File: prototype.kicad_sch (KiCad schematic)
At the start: 20 parts, among them CON1 SNES-CONN, IC1 SN74LVC4245A, IC2 SN74LVC4245A, IC3 SN74LVC4245A, IC4 SN74LVC4245A, IC5 SN74LVC4245A, IC6 SN74LVC4245A, IC7 SN74LVC4245A, U1 AMS1117-3.3

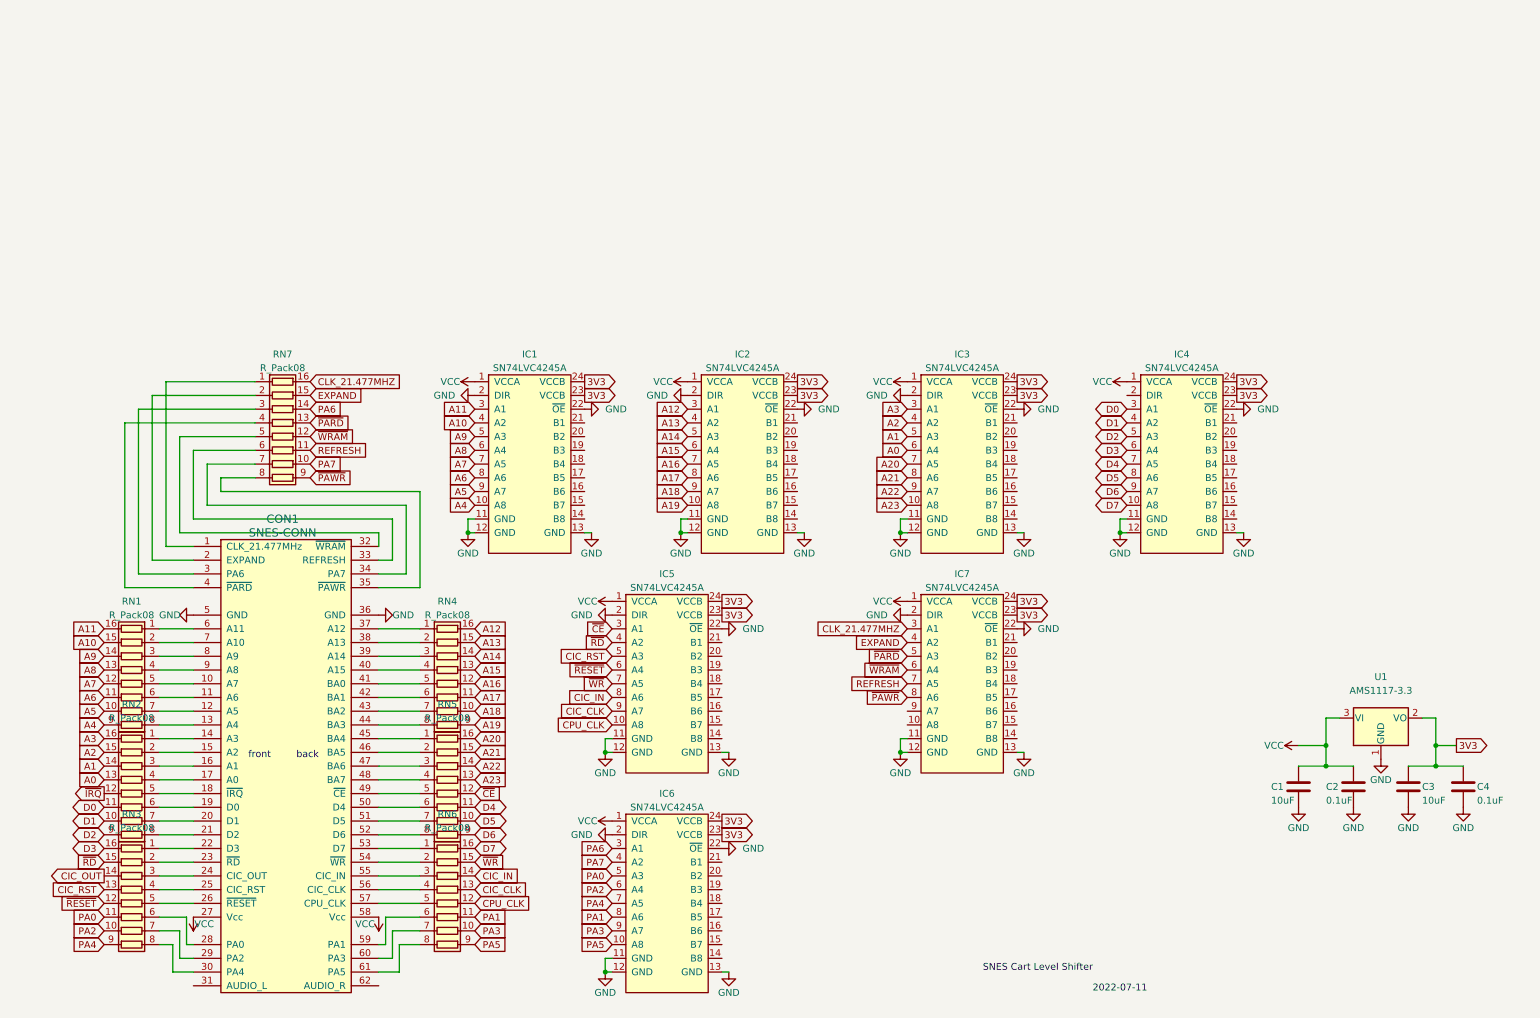
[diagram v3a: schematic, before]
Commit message: Redesign to reduce components, include PIC12 for CIC implementation
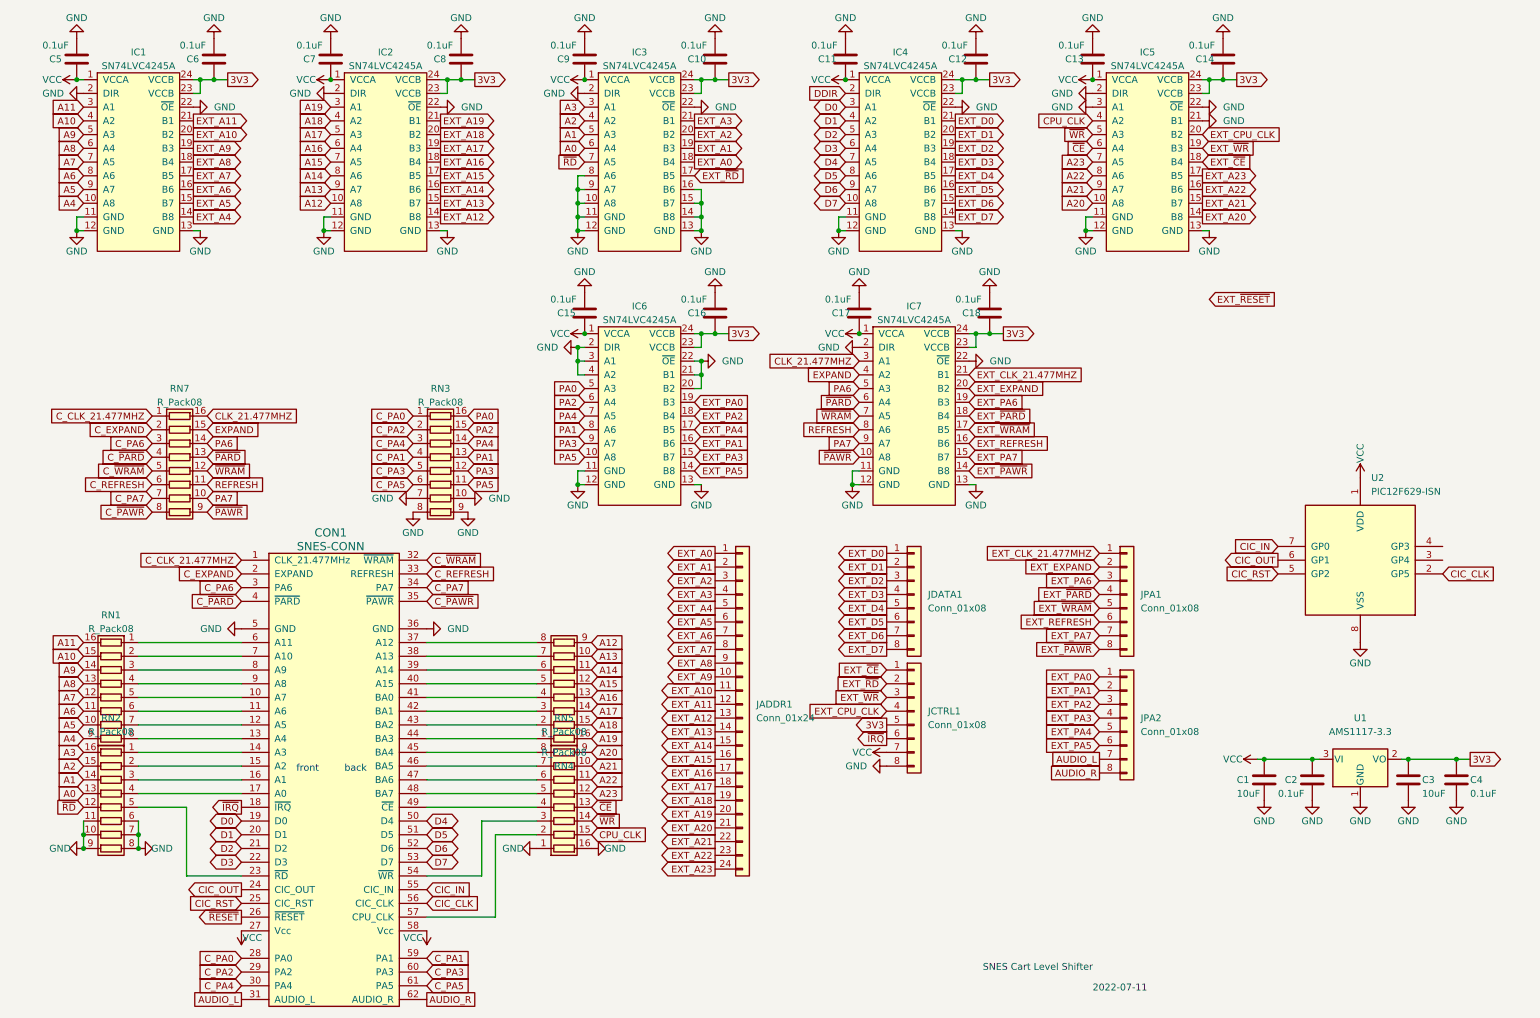
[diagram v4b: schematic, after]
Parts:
- removed RN6: R_Pack08, Package_SO:SOIC-16_3.9x9.9mm_P1.27mm, symbol Device:R_Pack08
- added C10, C11, C12, C13, C14, C15, C16, C17, C18, C5, C6, C7, C8, C9: 0.1uF, Capacitor_SMD:C_0805_2012Metric_Pad1.18x1.45mm_HandSolder, symbol Device:C
- added JADDR1: Conn_01x24, Connector_PinHeader_2.54mm:PinHeader_1x24_P2.54mm_Horizontal, symbol Connector_Generic:Conn_01x24
- added JCTRL1, JDATA1, JPA1, JPA2: Conn_01x08, Connector_PinHeader_2.54mm:PinHeader_1x08_P2.54mm_Horizontal, symbol Connector_Generic:Conn_01x08
- added U2: PIC12F629-ISN, Package_DIP:DIP-8_W7.62mm, symbol MCU_Microchip_PIC12:PIC12F629-ISN
- C1, C2, C3, C4: footprint Capacitor_SMD:C_1206_3216Metric -> Capacitor_SMD:C_0805_2012Metric_Pad1.18x1.45mm_HandSolder
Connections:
- net 3V3: now also C10.1, C12.1, C14.1, C16.1, C18.1, C6.1, C8.1, JCTRL1.5 (Pin_5)
- net A12: now also IC2.10 (A8), RN4.9 (R8.2); no longer IC2.3 (A1), RN4.16 (R1.2)
- net A13: now also IC2.9 (A7), RN4.10 (R7.2); no longer IC2.4 (A2), RN4.15 (R2.2)
- net A14: now also IC2.8 (A6), RN4.11 (R6.2); no longer IC2.5 (A3), RN4.14 (R3.2)
- net A15: now also IC2.7 (A5), RN4.12 (R5.2); no longer IC2.6 (A4), RN4.13 (R4.2)
- net A16: now also IC2.6 (A4), RN4.13 (R4.2); no longer IC2.7 (A5), RN4.12 (R5.2)
- net A17: now also IC2.5 (A3), RN4.14 (R3.2); no longer IC2.8 (A6), RN4.11 (R6.2)
- net A18: now also IC2.4 (A2), RN4.15 (R2.2); no longer IC2.9 (A7), RN4.10 (R7.2)
- net A19: now also IC2.3 (A1), RN4.16 (R1.2); no longer IC2.10 (A8), RN4.9 (R8.2)
- net A20: now also IC5.10 (A8), RN5.9 (R8.2); no longer IC3.7 (A5), RN5.16 (R1.2)
- net A21: now also IC5.9 (A7), RN5.10 (R7.2); no longer IC3.8 (A6), RN5.15 (R2.2)
- net A22: now also IC5.8 (A6), RN5.11 (R6.2); no longer IC3.9 (A7), RN5.14 (R3.2)
- net A23: now also IC5.7 (A5), RN5.12 (R5.2); no longer IC3.10 (A8), RN5.13 (R4.2)
- net CIC_CLK: now also CON1.56 (CIC_CLK), U2.2 (GP5); no longer IC5.9 (A7)
- net CIC_IN: now also CON1.55 (CIC_IN), U2.7 (GP0); no longer IC5.8 (A6)
- net CIC_OUT: now also CON1.24 (CIC_OUT), U2.6 (GP1); no longer RN3.14 (R3.2)
- net CIC_RST: now also CON1.25 (CIC_RST), U2.5 (GP2); no longer IC5.5 (A3), RN3.13 (R4.2)
- net CPU_CLK: now also IC5.4 (A2), RN5.15 (R2.2); no longer IC5.10 (A8)
- net D0: now also CON1.19 (D0); no longer RN2.11 (R6.2)
- net D1: now also CON1.20 (D1); no longer RN2.10 (R7.2)
- net D2: now also CON1.21 (D2); no longer RN2.9 (R8.2)
- net D3: now also CON1.22 (D3); no longer RN3.16 (R1.2)
- net D4: now also CON1.50 (D4); no longer RN5.11 (R6.2)
- net D5: now also CON1.51 (D5); no longer RN5.10 (R7.2)
- net D6: now also CON1.52 (D6); no longer RN5.9 (R8.2)
- net D7: now also CON1.53 (D7)
- net GND: now also IC3.10 (A8), IC3.14 (B8), IC3.15 (B7), IC3.16 (B6), IC3.8 (A6), IC3.9 (A7), IC5.21 (B1), IC5.3 (A1), IC6.20 (B2), IC6.21 (B1), IC6.3 (A1), IC6.4 (A2), RN2.10 (R7.2), RN2.11 (R6.2), RN2.6 (R6.1), RN2.7 (R7.1), RN2.8 (R8.1), RN2.9 (R8.2), RN3.10 (R7.2), RN3.7 (R7.1), RN3.8 (R8.1), RN3.9 (R8.2), RN5.1 (R1.1), RN5.16 (R1.2), C10.2, C11.2, C12.2, C13.2, C14.2, C15.2, C16.2, C17.2, C18.2, C5.2, C6.2, C7.2, C8.2, C9.2, JCTRL1.8 (Pin_8), U2.8 (VSS)
- net PA0: now also RN3.16 (R1.2); no longer RN3.11 (R6.2)
- net PA1: now also RN3.13 (R4.2)
- net PA2: now also RN3.15 (R2.2); no longer RN3.10 (R7.2)
- net PA3: now also RN3.12 (R5.2)
- net PA4: now also RN3.14 (R3.2); no longer RN3.9 (R8.2)
- net PA5: now also RN3.11 (R6.2)
- net PA6: now also IC7.5 (A3); no longer IC6.3 (A1)
- net PA7: now also IC7.9 (A7); no longer IC6.4 (A2)
- net REFRESH: now also IC7.8 (A6); no longer IC7.7 (A5)
- net VCC: now also C11.1, C13.1, C15.1, C17.1, C5.1, C7.1, C9.1, JCTRL1.7 (Pin_7), U2.1 (VDD)
- net ~{CE}: now also IC5.6 (A4), RN5.13 (R4.2); no longer IC5.3 (A1), RN5.12 (R5.2)
- net ~{IRQ}: now also CON1.18 (~{IRQ}), JCTRL1.6 (Pin_6); no longer RN2.12 (R5.2)
- net ~{PARD}: now also IC7.6 (A4); no longer IC7.5 (A3)
- net ~{PAWR}: now also IC7.10 (A8); no longer IC7.8 (A6)
- net ~{RD}: now also IC3.7 (A5), RN2.12 (R5.2); no longer IC5.4 (A2), RN3.15 (R2.2)
- net ~{RESET}: now also CON1.26 (~{RESET}); no longer IC5.6 (A4), RN3.12 (R5.2)
- net ~{WRAM}: now also IC7.7 (A5); no longer IC7.6 (A4)
- net ~{WR}: now also IC5.5 (A3), RN5.14 (R3.2); no longer IC5.7 (A5)
- net EXT_A20: now reaches IC5.14 (B8)
- net EXT_A20: now also JADDR1.21 (Pin_21)
- net EXT_A21: now reaches IC5.15 (B7)
- net EXT_A21: now also JADDR1.22 (Pin_22)
- net EXT_A22: now reaches IC5.16 (B6)
- net EXT_A22: now also JADDR1.23 (Pin_23)
- net EXT_A23: now reaches IC5.17 (B5)
- net EXT_A23: now also JADDR1.24 (Pin_24)
- net EXT_~{CE}: now reaches IC5.18 (B4)
- net EXT_~{CE}: now also JCTRL1.1 (Pin_1)
- net EXT_~{WR}: now reaches IC5.19 (B3)
- net EXT_~{WR}: now also JCTRL1.3 (Pin_3)
- net EXT_CPU_CLK: now reaches IC5.20 (B2)
- net EXT_CPU_CLK: now also JCTRL1.4 (Pin_4)
- net C_CLK_21.477MHZ: now reaches CON1.1 (CLK_21.477MHz), RN7.1 (R1.1)
- net at RN2.5 (R5.1): now also CON1.23 (~{RD}); no longer CON1.18 (~{IRQ})
- net C_EXPAND: now reaches CON1.2 (EXPAND), RN7.2 (R2.1)
- net C_PA0: now reaches RN3.1 (R1.1)
- net C_PA0: now also CON1.28 (PA0); no longer CON1.22 (D3)
- net C_PA2: now reaches RN3.2 (R2.1)
- net C_PA2: now also CON1.29 (PA2); no longer CON1.23 (~{RD})
- net C_PA4: now reaches RN3.3 (R3.1)
- net C_PA4: now also CON1.30 (PA4); no longer CON1.24 (CIC_OUT)
- net C_PA1: now reaches RN3.4 (R4.1)
- net C_PA1: now also CON1.59 (PA1); no longer CON1.25 (CIC_RST)
- net C_PA3: now reaches RN3.5 (R5.1)
- net C_PA3: now also CON1.60 (PA3); no longer CON1.26 (~{RESET})
- net C_PA5: now reaches RN3.6 (R6.1)
- net C_PA5: now also CON1.61 (PA5); no longer CON1.28 (PA0)
- net C_PA6: now reaches CON1.3 (PA6), RN7.3 (R3.1)
- net AUDIO_L: now reaches CON1.31 (AUDIO_L)
- net AUDIO_L: now also JPA2.7 (Pin_7)
- net C_~{WRAM}: now reaches CON1.32 (~{WRAM}), RN7.5 (R5.1)
- net C_REFRESH: now reaches CON1.33 (REFRESH), RN7.6 (R6.1)
- net C_PA7: now reaches CON1.34 (PA7), RN7.7 (R7.1)
- net C_~{PAWR}: now reaches CON1.35 (~{PAWR}), RN7.8 (R8.1)
- net at CON1.37 (A12): now also RN4.8 (R8.1); no longer RN4.1 (R1.1)
- net at CON1.38 (A13): now also RN4.7 (R7.1); no longer RN4.2 (R2.1)
- net at CON1.39 (A14): now also RN4.6 (R6.1); no longer RN4.3 (R3.1)
- net C_~{PARD}: now reaches CON1.4 (~{PARD}), RN7.4 (R4.1)
- net at CON1.40 (A15): now also RN4.5 (R5.1); no longer RN4.4 (R4.1)
- net at CON1.41 (BA0): now also RN4.4 (R4.1); no longer RN4.5 (R5.1)
- net at CON1.42 (BA1): now also RN4.3 (R3.1); no longer RN4.6 (R6.1)
- net at CON1.43 (BA2): now also RN4.2 (R2.1); no longer RN4.7 (R7.1)
- net at CON1.44 (BA3): now also RN4.1 (R1.1); no longer RN4.8 (R8.1)
- net at CON1.45 (BA4): now also RN5.8 (R8.1); no longer RN5.1 (R1.1)
- net at CON1.46 (BA5): now also RN5.7 (R7.1); no longer RN5.2 (R2.1)
- net at CON1.47 (BA6): now also RN5.6 (R6.1); no longer RN5.3 (R3.1)
- net at CON1.48 (BA7): now also RN5.5 (R5.1); no longer RN5.4 (R4.1)
- net at CON1.49 (~{CE}): now also RN5.4 (R4.1); no longer RN5.5 (R5.1)
- net at CON1.54 (~{WR}): now also RN5.3 (R3.1)
- net at CON1.57 (CPU_CLK): now also RN5.2 (R2.1)
- net AUDIO_R: now reaches CON1.62 (AUDIO_R)
- net AUDIO_R: now also JPA2.8 (Pin_8)
- net EXT_D7: now reaches IC4.14 (B8)
- net EXT_D7: now also JDATA1.8 (Pin_8)
- net EXT_D6: now reaches IC4.15 (B7)
- net EXT_D6: now also JDATA1.7 (Pin_7)
- net EXT_D5: now reaches IC4.16 (B6)
- net EXT_D5: now also JDATA1.6 (Pin_6)
- net EXT_D4: now reaches IC4.17 (B5)
- net EXT_D4: now also JDATA1.5 (Pin_5)
- net EXT_D3: now reaches IC4.18 (B4)
- net EXT_D3: now also JDATA1.4 (Pin_4)
- net EXT_D2: now reaches IC4.19 (B3)
- net EXT_D2: now also JDATA1.3 (Pin_3)
- net DDIR: now reaches IC4.2 (DIR)
- net EXT_D1: now reaches IC4.20 (B2)
- net EXT_D1: now also JDATA1.2 (Pin_2)
- net EXT_D0: now reaches IC4.21 (B1)
- net EXT_D0: now also JDATA1.1 (Pin_1)
- net EXT_A4: now reaches IC1.14 (B8)
- net EXT_A4: now also JADDR1.5 (Pin_5)
- net EXT_A5: now reaches IC1.15 (B7)
- net EXT_A5: now also JADDR1.6 (Pin_6)
- net EXT_A6: now reaches IC1.16 (B6)
- net EXT_A6: now also JADDR1.7 (Pin_7)
- net EXT_A7: now reaches IC1.17 (B5)
- net EXT_A7: now also JADDR1.8 (Pin_8)
- net EXT_A8: now reaches IC1.18 (B4)
- net EXT_A8: now also JADDR1.9 (Pin_9)
- net EXT_A9: now reaches IC1.19 (B3)
- net EXT_A9: now also JADDR1.10 (Pin_10)
- net EXT_A10: now reaches IC1.20 (B2)
- net EXT_A10: now also JADDR1.11 (Pin_11)
- net EXT_A11: now reaches IC1.21 (B1)
- net EXT_A11: now also JADDR1.12 (Pin_12)
- net EXT_A12: now reaches IC2.14 (B8)
- net EXT_A12: now also JADDR1.13 (Pin_13)
- net EXT_A13: now reaches IC2.15 (B7)
- net EXT_A13: now also JADDR1.14 (Pin_14)
- net EXT_A14: now reaches IC2.16 (B6)
- net EXT_A14: now also JADDR1.15 (Pin_15)
- net EXT_A15: now reaches IC2.17 (B5)
- net EXT_A15: now also JADDR1.16 (Pin_16)
- net EXT_A16: now reaches IC2.18 (B4)
- net EXT_A16: now also JADDR1.17 (Pin_17)
- net EXT_A17: now reaches IC2.19 (B3)
- net EXT_A17: now also JADDR1.18 (Pin_18)
- net EXT_A18: now reaches IC2.20 (B2)
- net EXT_A18: now also JADDR1.19 (Pin_19)
- net EXT_A19: now reaches IC2.21 (B1)
- net EXT_A19: now also JADDR1.20 (Pin_20)
- net EXT_~{PAWR}: now reaches IC7.14 (B8)
- net EXT_~{PAWR}: now also JPA1.8 (Pin_8)
- net EXT_PA7: now reaches IC7.15 (B7)
- net EXT_PA7: now also JPA1.7 (Pin_7)
- net EXT_REFRESH: now reaches IC7.16 (B6)
- net EXT_REFRESH: now also JPA1.6 (Pin_6)
- net EXT_~{WRAM}: now reaches IC7.17 (B5)
- net EXT_~{WRAM}: now also JPA1.5 (Pin_5)
- net EXT_~{PARD}: now reaches IC7.18 (B4)
- net EXT_~{PARD}: now also JPA1.4 (Pin_4)
- net EXT_PA6: now reaches IC7.19 (B3)
- net EXT_PA6: now also JPA1.3 (Pin_3)
- net EXT_EXPAND: now reaches IC7.20 (B2)
- net EXT_EXPAND: now also JPA1.2 (Pin_2)
- net EXT_CLK_21.477MHZ: now reaches IC7.21 (B1)
- net EXT_CLK_21.477MHZ: now also JPA1.1 (Pin_1)
- net EXT_PA5: now reaches IC6.14 (B8)
- net EXT_PA5: now also JPA2.6 (Pin_6)
- net EXT_PA3: now reaches IC6.15 (B7)
- net EXT_PA3: now also JPA2.4 (Pin_4)
- net EXT_PA1: now reaches IC6.16 (B6)
- net EXT_PA1: now also JPA2.2 (Pin_2)
- net EXT_PA4: now reaches IC6.17 (B5)
- net EXT_PA4: now also JPA2.5 (Pin_5)
- net EXT_PA2: now reaches IC6.18 (B4)
- net EXT_PA2: now also JPA2.3 (Pin_3)
- net EXT_PA0: now reaches IC6.19 (B3)
- net EXT_PA0: now also JPA2.1 (Pin_1)
- net EXT_~{RD}: now reaches IC3.17 (B5)
- net EXT_~{RD}: now also JCTRL1.2 (Pin_2)
- net EXT_A0: now reaches IC3.18 (B4)
- net EXT_A0: now also JADDR1.1 (Pin_1)
- net EXT_A1: now reaches IC3.19 (B3)
- net EXT_A1: now also JADDR1.2 (Pin_2)
- net EXT_A2: now reaches IC3.20 (B2)
- net EXT_A2: now also JADDR1.3 (Pin_3)
- net EXT_A3: now reaches IC3.21 (B1)
- net EXT_A3: now also JADDR1.4 (Pin_4)
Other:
- moved on the sheet: C1, C2, CON1, IC1, IC2, IC3, IC4, IC5, IC6, IC7, RN1, RN2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

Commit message: Routed PCB; fixed up labels on schematic for proper input/output direction; added back in IRQ and RESET as inputs, can easily pull down with mosfet later
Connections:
- net EXT_CPU_CLK: now also JCTRL1.5 (Pin_5); no longer JCTRL1.4 (Pin_4)
- net EXT_~{RD}: now also IC3.16 (B6), JCTRL1.4 (Pin_4); no longer IC3.17 (B5), JCTRL1.2 (Pin_2)
- net EXT_~{RESET}: now also IC3.15 (B7), JCTRL1.6 (Pin_6)
- net GND: no longer IC3.15 (B7), IC3.16 (B6), IC3.8 (A6), IC3.9 (A7), RN2.10 (R7.2), RN2.11 (R6.2), RN2.6 (R6.1), RN2.7 (R7.1)
- net VCC: no longer JCTRL1.7 (Pin_7)
- net ~{IRQ}: now also IC3.7 (A5), RN2.12 (R5.2); no longer CON1.18 (~{IRQ}), JCTRL1.6 (Pin_6)
- net ~{RD}: now also IC3.8 (A6), RN2.11 (R6.2); no longer IC3.7 (A5), RN2.12 (R5.2)
- net ~{RESET}: now also IC3.9 (A7), RN2.10 (R7.2); no longer CON1.26 (~{RESET})
- net at RN2.5 (R5.1): now also CON1.18 (~{IRQ}); no longer CON1.23 (~{RD})
- net 3V3 renamed +3.3V
- net +3.3V: now also JCTRL1.7 (Pin_7); no longer JCTRL1.5 (Pin_5)
- new net: CON1.23 (~{RD}), RN2.6 (R6.1)
- new net: CON1.26 (~{RESET}), RN2.7 (R7.1)
- new net EXT_~{IRQ}: IC3.17 (B5), JCTRL1.2 (Pin_2)

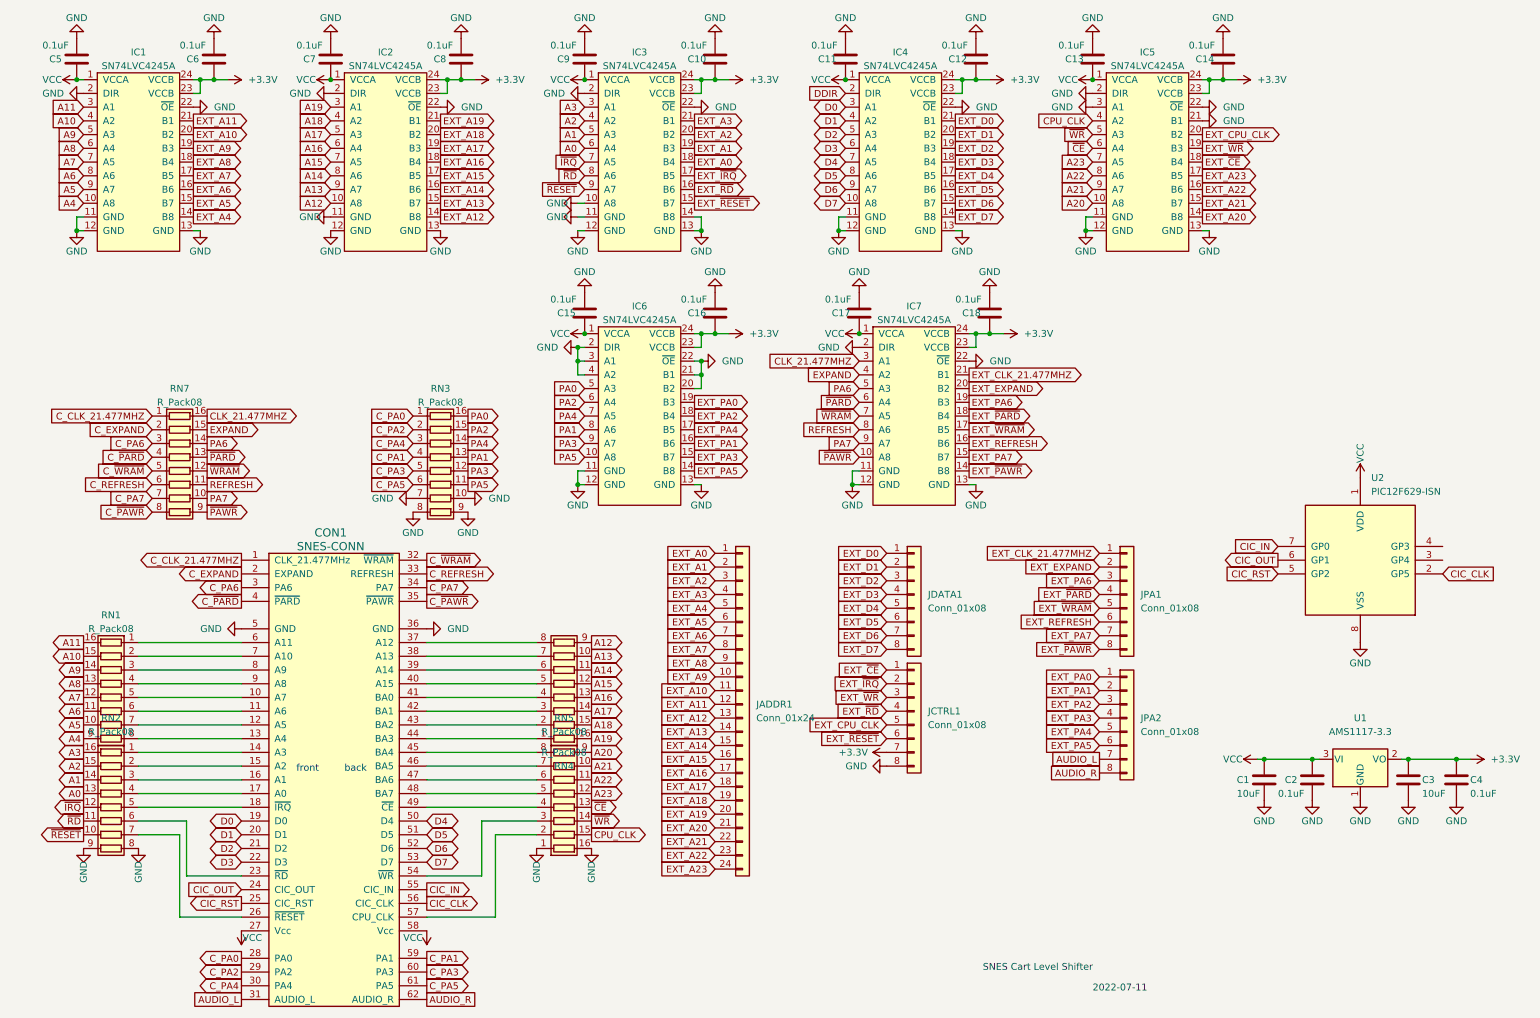
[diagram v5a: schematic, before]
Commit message: Routed new connector dedicated to power pins; routed DDIR pin to header
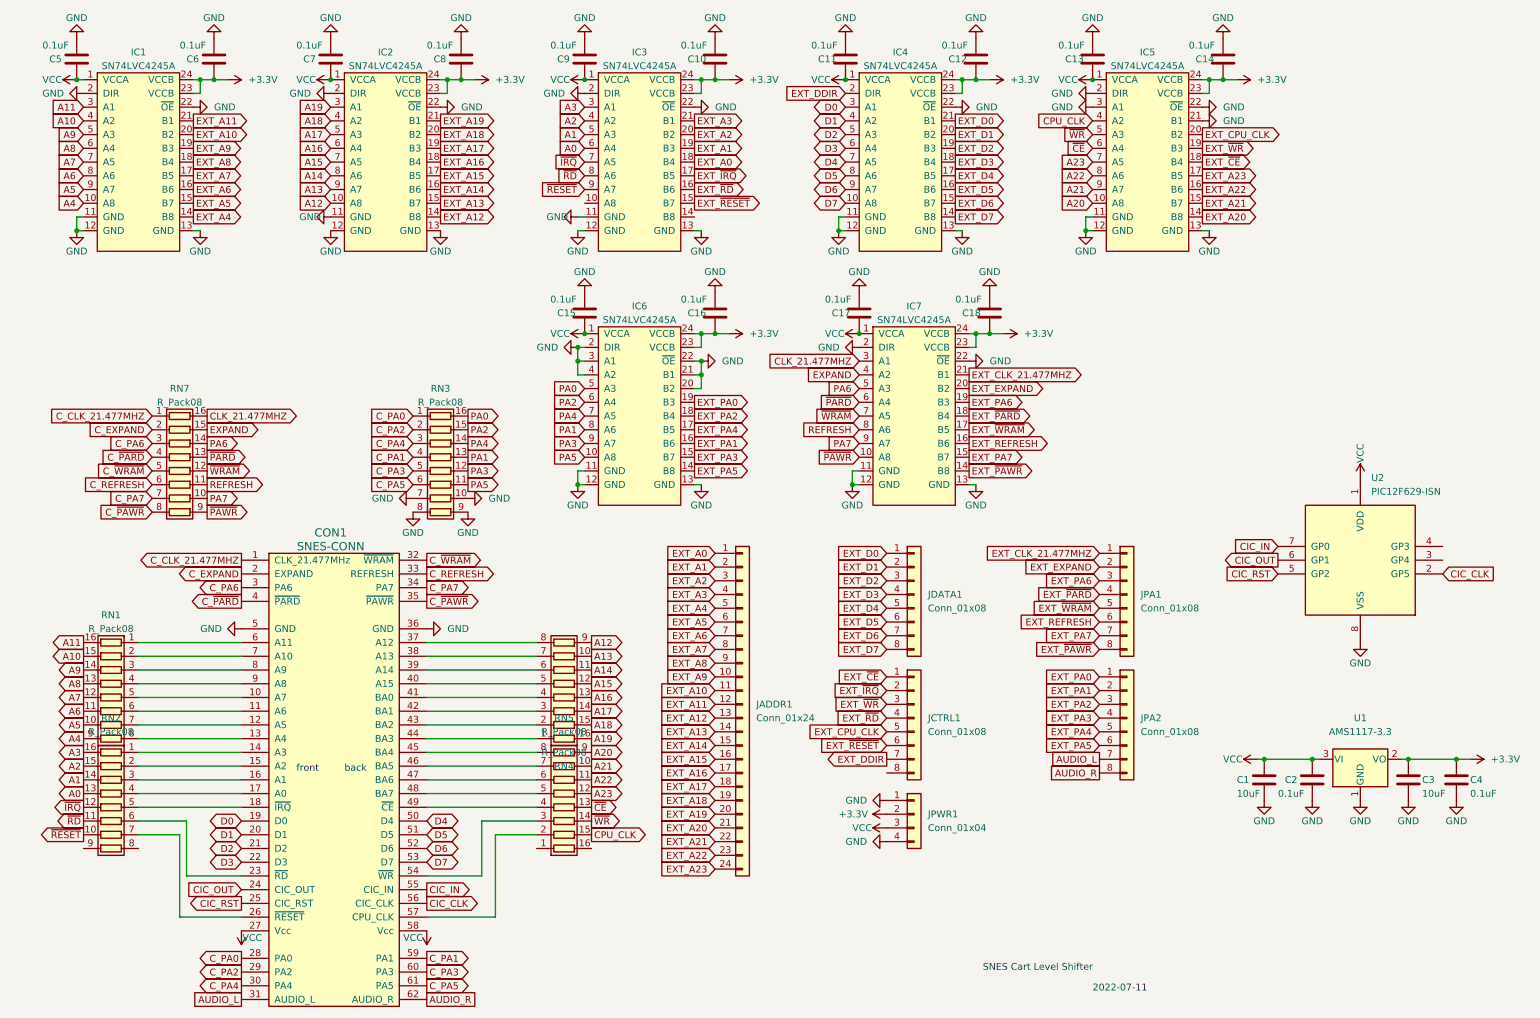
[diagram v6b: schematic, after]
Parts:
- added JPWR1: Conn_01x04, Connector_PinHeader_2.54mm:PinHeader_1x04_P2.54mm_Horizontal, symbol Connector_Generic:Conn_01x04
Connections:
- net +3.3V: now also JPWR1.2 (Pin_2); no longer JCTRL1.7 (Pin_7)
- net GND: now also JPWR1.1 (Pin_1), JPWR1.4 (Pin_4); no longer IC3.10 (A8), IC3.14 (B8), JCTRL1.8 (Pin_8), RN2.8 (R8.1), RN2.9 (R8.2), RN5.1 (R1.1), RN5.16 (R1.2)
- net VCC: now also JPWR1.3 (Pin_3)
- net DDIR renamed EXT_DDIR
- net EXT_DDIR: now also JCTRL1.7 (Pin_7)
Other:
- moved on the sheet: JCTRL1
